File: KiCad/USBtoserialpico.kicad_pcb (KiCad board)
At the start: 2 copper layers, 80.7 x 35.1 mm, 26 parts, among them J1 Conn_01x04_Male, J2 Conn_01x02_Male, J3 Conn_01x05_Male, SW1 SW_DIP_x06, SW2 SW_MEC_5E, U1 MAX232, U2 PICO_RP2040

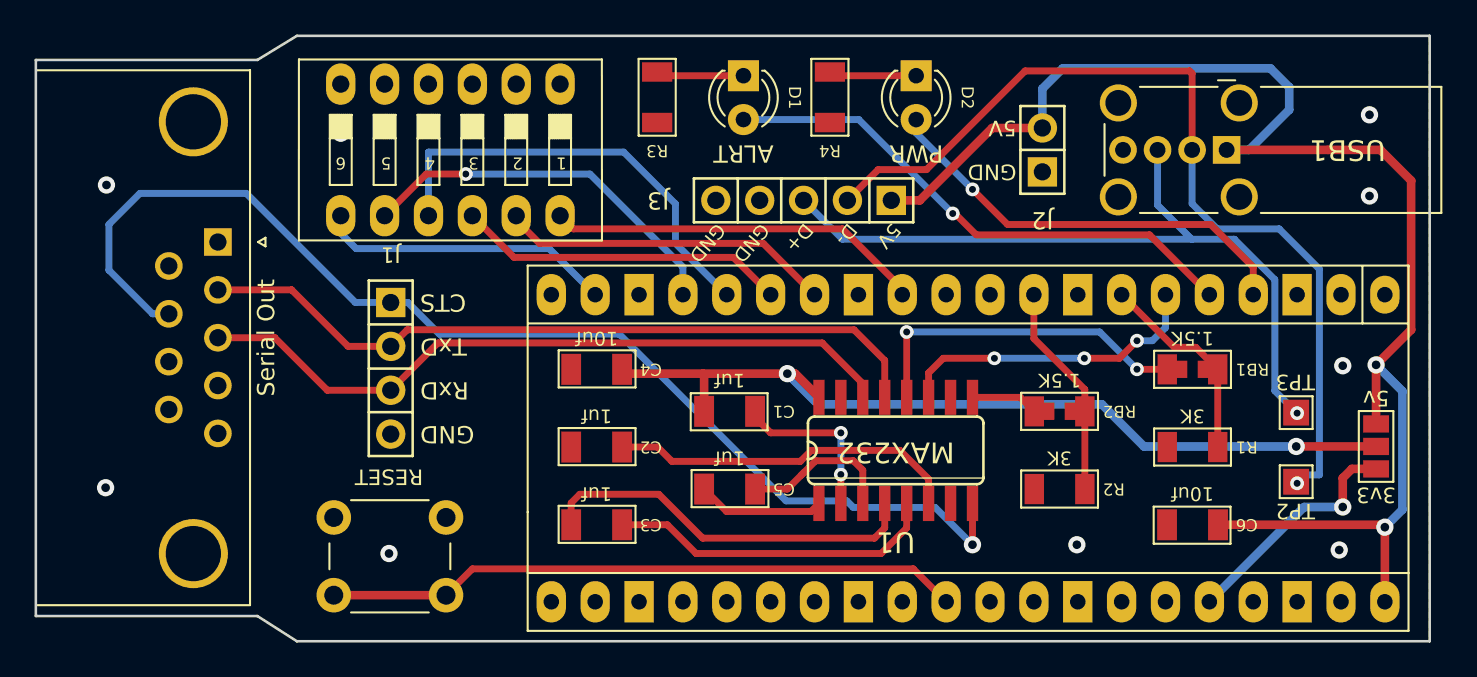
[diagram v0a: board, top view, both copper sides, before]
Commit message: fixed some small mistakes in the pcb
I forgot to give the max232 a connection to ground.
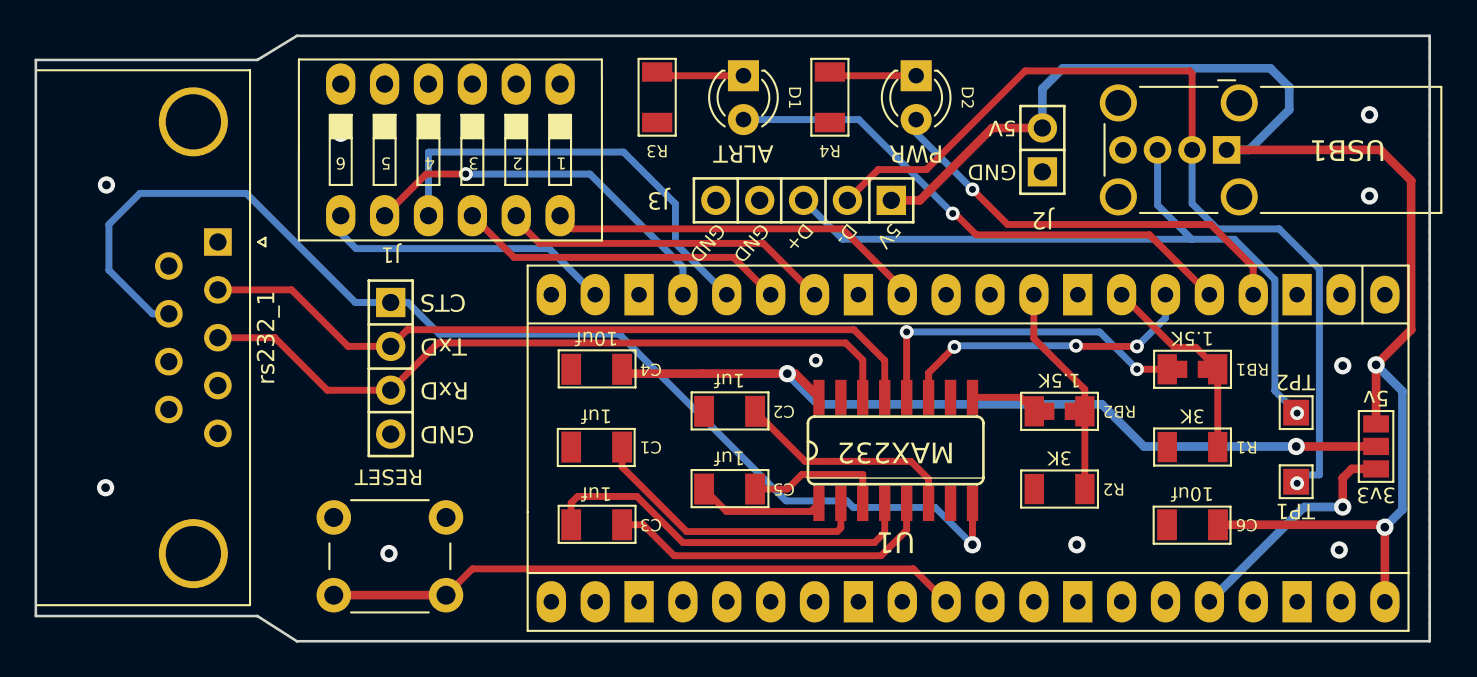
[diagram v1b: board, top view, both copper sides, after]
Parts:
- rs232_1: renamed from Serial Out
- moved C1 7.97 mm to (153.5, 99.5)
- moved C2 7.97 mm to (161.2, 97.4)
- renumbered TP2 to TP1, TP3 to TP2
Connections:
- C1 pad 2: Net-(C1-Pad2) -> GND
- C4 pad 2: Net-(C1-Pad2) -> Net-(C4-Pad2)
- JP1 pad 2: Net-(C1-Pad2) -> Net-(C4-Pad2)
- U1 pad 16: Net-(C1-Pad2) -> Net-(C4-Pad2)
- rs232_1 pad 0: GND -> Net-(rs232_1-Pad0)
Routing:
- net Net-(C1-Pad2): track 50.1 -> 0.00 mm, vias 2 -> 0
- net Net-(C4-Pad2): track 0.00 -> 47.9 mm, vias 0 -> 2
- net Net-(C1-Pad1): track 9.77 -> 16.9 mm, vias 2 -> 0
- net Net-(C2-Pad2): track 20.5 -> 13.4 mm
- net Net-(J1-Pad3): track 41.5 -> 43.1 mm
- net Net-(C5-Pad2): track 9.27 -> 8.26 mm
- net GND: vias 9 -> 10
